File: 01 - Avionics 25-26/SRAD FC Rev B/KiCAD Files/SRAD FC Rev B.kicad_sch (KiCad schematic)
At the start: 2 parts, among them J1 Conn_ARM_SWD_TagConnect_TC2030

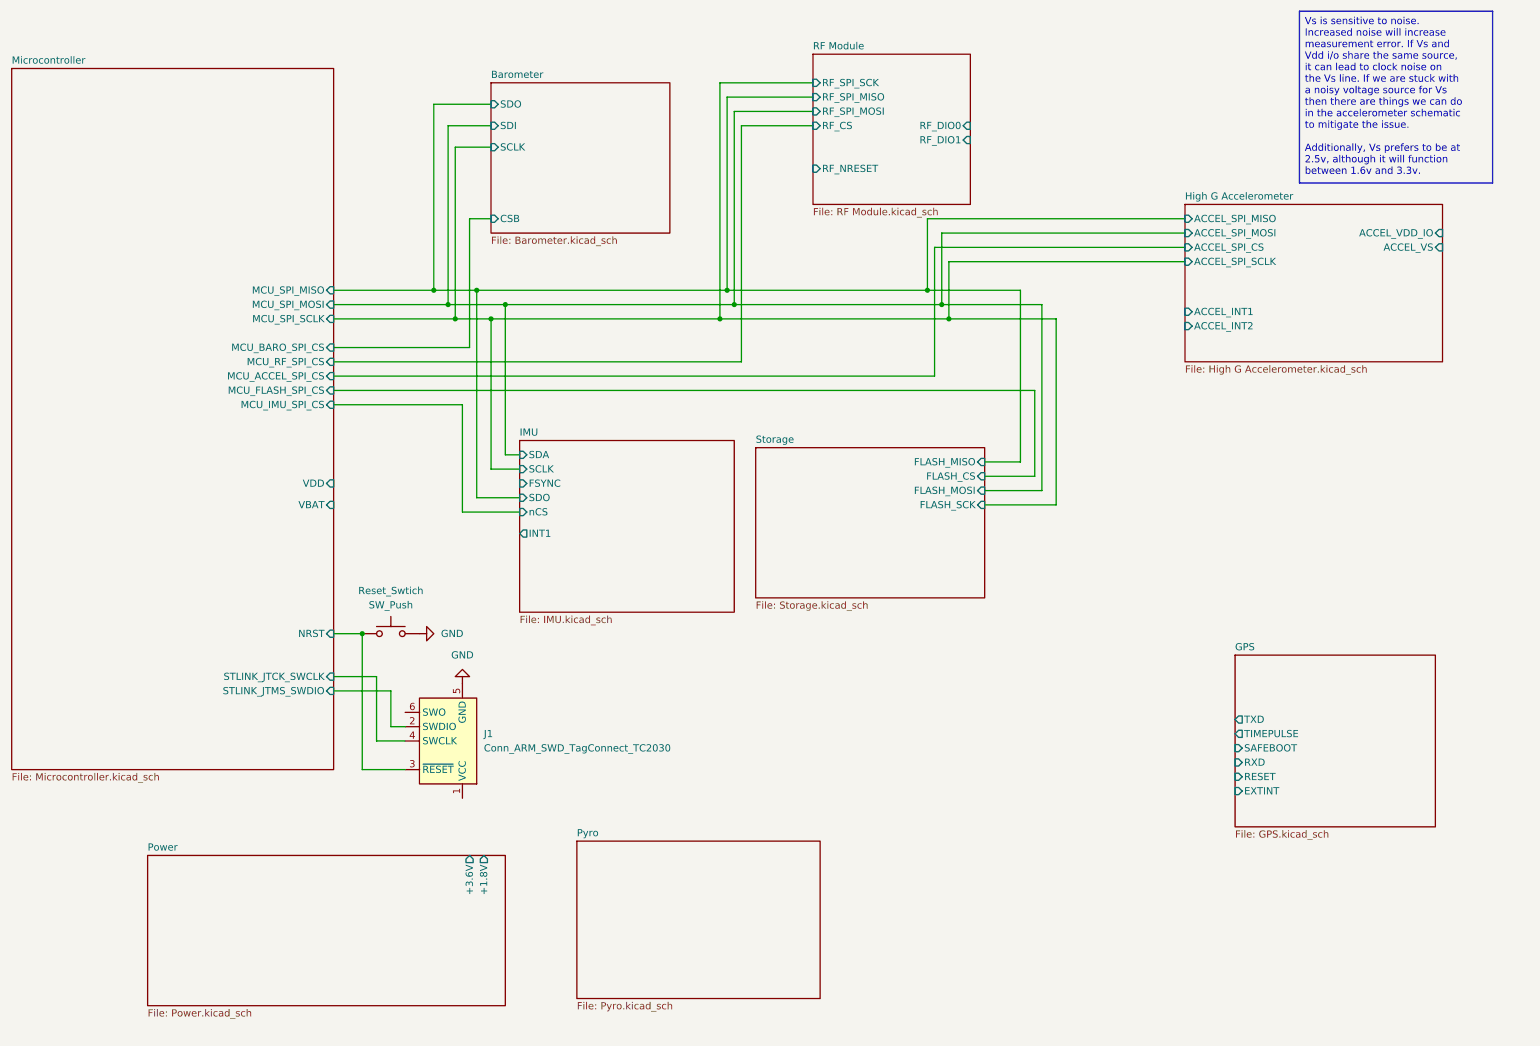
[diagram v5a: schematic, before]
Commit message: wired gps uart
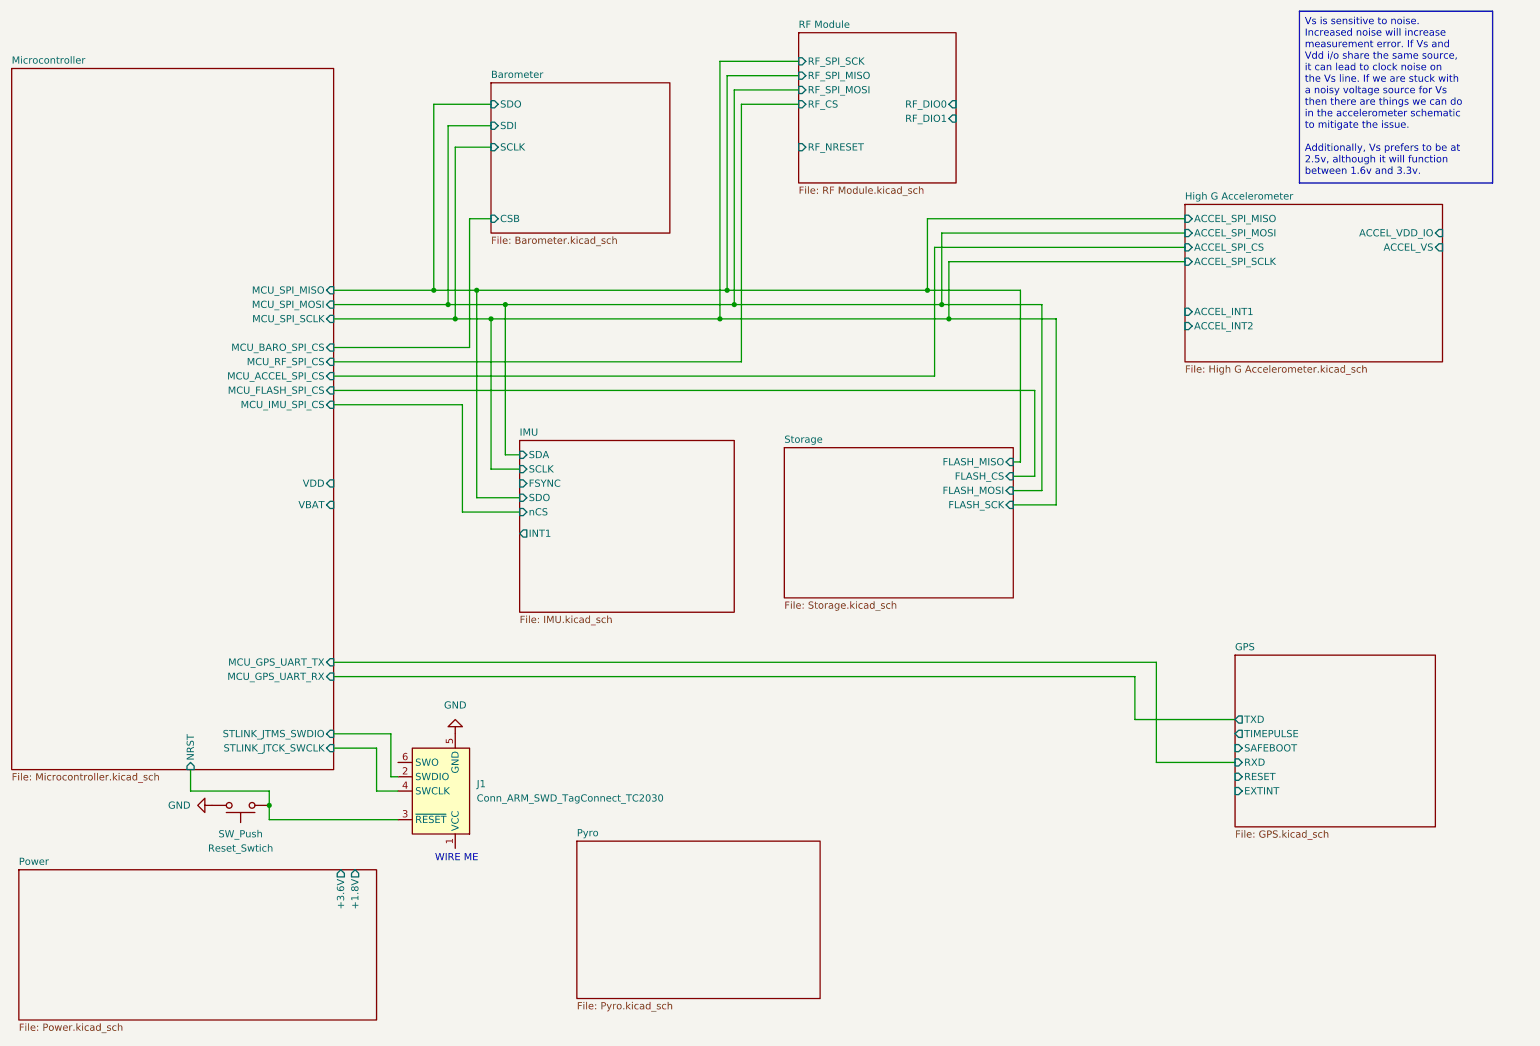
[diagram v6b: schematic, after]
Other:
- sheet Microcontroller ports: added MCU_GPS_UART_RX, MCU_GPS_UART_TX; removed none
- note added: "WIRE ME"
- moved on the sheet: J1, Reset_Swtich

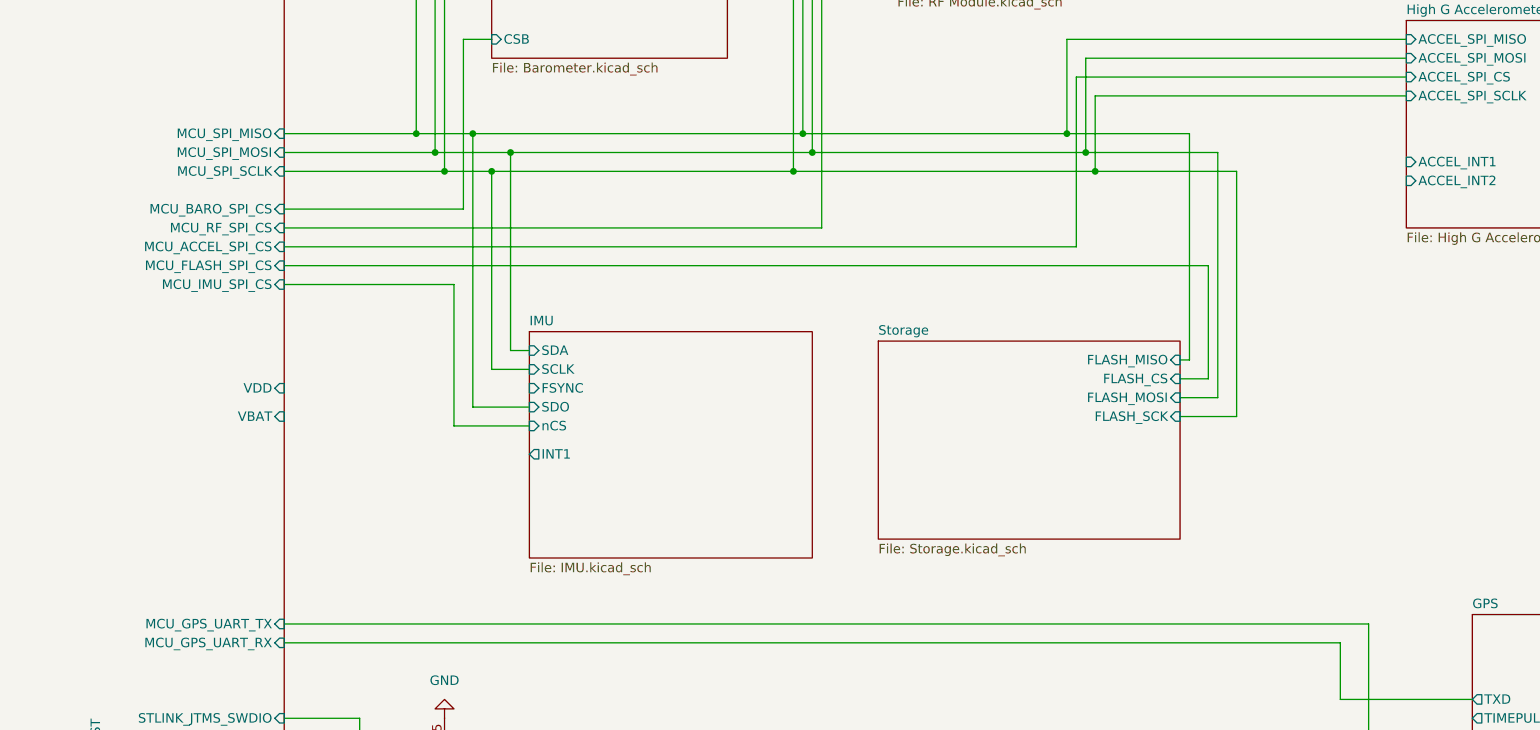
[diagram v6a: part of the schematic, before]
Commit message: wired interrupt sources
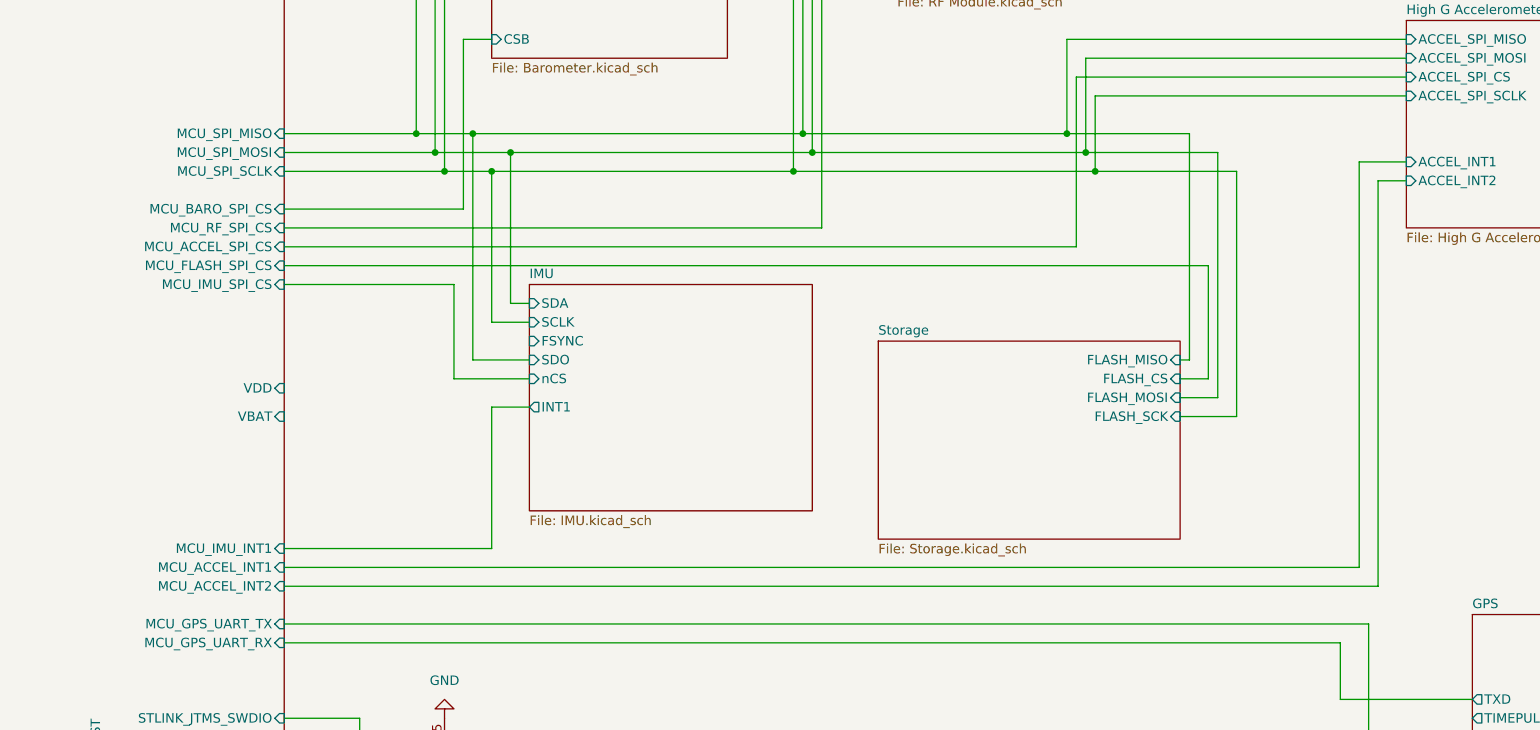
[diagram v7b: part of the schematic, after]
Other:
- sheet Microcontroller ports: added MCU_ACCEL_INT1, MCU_ACCEL_INT2, MCU_IMU_INT1; removed none
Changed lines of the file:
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@@
+	(wire
+		(pts
+			(xy 106.68 118.11) (xy 106.68 99.06)
+		)
+		(stroke
+			(width 0)
+			(type default)
+		)
+	)
+	(wire
+		(pts
+			(xy 106.68 99.06) (xy 111.76 99.06)
+		)
+		(stroke
+			(width 0)
+			(type default)
+		)
+	)
 	(wire
 		(pts
@@
 	(wire
 		(pts
-			(xy 106.68 93.98) (xy 111.76 93.98)
-		)
-		(stroke
-			(width 0)
-			(type default)
-		)
-	)
-	(wire
-		(pts
-			(xy 109.22 91.44) (xy 111.76 91.44)
-		)
-		(stroke
-			(width 0)
-			(type default)
-		)
-	)
-	(wire
-		(pts
-			(xy 106.68 67.31) (xy 106.68 93.98)
+			(xy 106.68 87.63) (xy 111.76 87.63)
+		)
+		(stroke
+			(width 0)
+			(type default)
+		)
+	)
+	(wire
+		(pts
+			(xy 109.22 85.09) (xy 111.76 85.09)
+		)
+		(stroke
+			(width 0)
+			(type default)
+		)
+	)
+	(wire
+		(pts
+			(xy 106.68 67.31) (xy 106.68 87.63)
+		)
+		(stroke
+			(width 0)
+			(type default)
+		)
+	)
+	(wire
+		(pts
+			(xy 223.52 120.65) (xy 223.52 66.04)
 		)
 		(stroke
@@
 	(wire
 		(pts
+			(xy 78.74 123.19) (xy 226.06 123.19)
+		)
+		(stroke
+			(width 0)
+			(type default)
+		)
+	)
+	(wire
+		(pts
 			(xy 186.69 64.77) (xy 186.69 52.07)
 		)
@@
 	(wire
 		(pts
+			(xy 226.06 68.58) (xy 229.87 68.58)
+		)
+		(stroke
+			(width 0)
+			(type default)
+		)
+	)
+	(wire
+		(pts
 			(xy 220.98 138.43) (xy 238.76 138.43)
 		)
@@
 	(wire
 		(pts
-			(xy 109.22 64.77) (xy 109.22 91.44)
+			(xy 109.22 64.77) (xy 109.22 85.09)
 		)
 		(stroke
@@
 	(wire
 		(pts
-			(xy 104.14 62.23) (xy 104.14 99.06)
+			(xy 104.14 62.23) (xy 104.14 92.71)
 		)
 		(stroke
@@
 	(wire
 		(pts
+			(xy 78.74 118.11) (xy 106.68 118.11)
+		)
+		(stroke
+			(width 0)
+			(type default)
+		)
+	)
+	(wire
+		(pts
 			(xy 78.74 72.39) (xy 102.87 72.39)
 		)
@@
 	(wire
 		(pts
-			(xy 101.6 101.6) (xy 111.76 101.6)
-		)
-		(stroke
-			(width 0)
-			(type default)
-		)
-	)
-	(wire
-		(pts
-			(xy 104.14 99.06) (xy 111.76 99.06)
+			(xy 101.6 95.25) (xy 111.76 95.25)
+		)
+		(stroke
+			(width 0)
+			(type default)
+		)
+	)
+	(wire
+		(pts
+			(xy 104.14 92.71) (xy 111.76 92.71)
 		)
 		(stroke
@@
 	(wire
 		(pts
+			(xy 78.74 120.65) (xy 223.52 120.65)
+		)
+		(stroke
+			(width 0)
+			(type default)
+		)
+	)
+	(wire
+		(pts
 			(xy 67.31 156.21) (xy 67.31 153.67)
 		)
@@
 	(wire
 		(pts
+			(xy 223.52 66.04) (xy 229.87 66.04)
+		)
+		(stroke
+			(width 0)
+			(type default)
+		)
+	)
+	(wire
+		(pts
 			(xy 67.31 151.13) (xy 67.31 153.67)
 		)
@@
 	(wire
 		(pts
-			(xy 101.6 82.55) (xy 101.6 101.6)
+			(xy 226.06 123.19) (xy 226.06 68.58)
+		)
+		(stroke
+			(width 0)
+			(type default)
+		)
+	)
+	(wire
+		(pts
+			(xy 101.6 82.55) (xy 101.6 95.25)
 		)
 		(stroke
@@
 			)
 		)
+		(pin "MCU_ACCEL_INT2" input
+			(at 78.74 123.19 0)
+			(effects
+				(font
+					(size 1.27 1.27)
+				)
+				(justify right)
+			)
+		)
+		(pin "MCU_IMU_INT1" input
+			(at 78.74 118.11 0)
+			(effects
+				(font
+					(size 1.27 1.27)
+				)
+				(justify right)
+			)
+		)
+		(pin "MCU_ACCEL_INT1" input
+			(at 78.74 120.65 0)
+			(effects
+				(font
+					(size 1.27 1.27)
+				)
+				(justify right)
+			)
+		)
 		(instances
 			(project "SRAD FC Rev B"
@@
 	)
 	(sheet
-		(at 111.76 88.9)
+		(at 111.76 82.55)
 		(size 38.1 30.48)
 		(exclude_from_sim no)
@@
 		)
 		(property "Sheetname" "IMU"
-			(at 111.76 88.1884 0)
+			(at 111.76 81.8384 0)
 			(effects
 				(font
@@
 		)
 		(property "Sheetfile" "IMU.kicad_sch"
-			(at 111.76 119.9646 0)
+			(at 111.76 113.6146 0)
 			(effects
 				(font
@@
 		)
 		(pin "SDA" input
-			(at 111.76 91.44 180)
+			(at 111.76 85.09 180)
 			(effects
 				(font
@@
 		)
 		(pin "SCLK" input
-			(at 111.76 93.98 180)
+			(at 111.76 87.63 180)
 			(effects
 				(font
@@
 		)
 		(pin "FSYNC" input
-			(at 111.76 96.52 180)
+			(at 111.76 90.17 180)
 			(effects
 				(font
@@
 		)
 		(pin "SDO" input
+			(at 111.76 92.71 180)
+			(effects
+				(font
+					(size 1.27 1.27)
+				)
+				(justify left)
+			)
+		)
+		(pin "INT1" output
 			(at 111.76 99.06 180)
 			(effects
@@
 			)
 		)
-		(pin "INT1" output
-			(at 111.76 105.41 180)
-			(effects
-				(font
-					(size 1.27 1.27)
-				)
-				(justify left)
-			)
-		)
 		(pin "nCS" input
-			(at 111.76 101.6 180)
-			(effects
-				(font
+			(at 111.76 95.25 180)
+			(effects
+				(font

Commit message: moved..... stuff
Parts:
- removed J1: Conn_ARM_SWD_TagConnect_TC2030, Connector:Tag-Connect_TC2030-IDC-FP_2x03_P1.27mm_Vertical, symbol Connector:Conn_ARM_SWD_TagConnect_TC2030
- removed Reset_Swtich: SW_Push, symbol Switch:SW_Push
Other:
- sheet High G Accelerometer ports: added none; removed ACCEL_VDD_IO, ACCEL_VS
- sheet Microcontroller ports: added none; removed STLINK_JTCK_SWCLK, STLINK_JTMS_SWDIO
- note removed: "WIRE ME"
